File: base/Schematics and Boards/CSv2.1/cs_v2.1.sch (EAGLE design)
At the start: 80 parts, among them J101 J-JTAG-CORTEX-NEEDLE6-LEGS, J301 HIROSE-DF40_44-PIN_CONNECTORS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, J302 HIROSE-DF40_30-PIN_CONNECTORS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, Q201 FK3303010L, Q202 DMG3415UFY4Q-7F, Q203 FK3303010L, Q204 FK3303010L, U101 ATSAMD51, U102 AT25SF641-MHB-T, U201 COULOMB-MAX17262, U202 MAX77827BEWC+T, U203 SENSOR-SI7006, U204 LOADSWITCH-MIC94164, U205 LOADSWITCH-MIC94164, Y101 16M, Y102 ABS07-32.768KHZ-9-T

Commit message: Minor modifications from learnings of debug-board build
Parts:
- DTR, PROC, STOR, TEMP: value TPTP06R -> PTR1TP10SQ; device TestPoints:TPTP06R -> TestPoints:PTR1TP10SQ
- J301: value HIROSE-DF40_44-PIN_CONNECTORS-RECEPTACLE -> HIROSE-DF40_50-PIN_CONNECTORS-RECEPTACLE; device Connectors:HIROSE-DF40_44-PIN_CONNECTORS-RECEPTACLE -> Connectors:HIROSE-DF40_50-PIN_CONNECTORS-RECEPTACLE
- J302: value HIROSE-DF40_30-PIN_CONNECTORS-RECEPTACLE -> HIROSE-DF40_50-PIN_CONNECTORS-RECEPTACLE; device Connectors:HIROSE-DF40_30-PIN_CONNECTORS-RECEPTACLE -> Connectors:HIROSE-DF40_50-PIN_CONNECTORS-RECEPTACLE
- R206: value 1 -> 2.21; MANUFACTURER (none) -> Stackpole; PART_NO ERJ-3RQF1R0V -> RNCF0603BKC2R21; TOL 1% -> 0.1%
- R207: MANUFACTURER (none) -> Ohmite; PART_NO ERJ-3BQFR51V -> KDV06DR510ET; TOL 1% -> 0.5%
- R208: MANUFACTURER (none) -> KOA Speer; PART_NO ERJ-3RQF1R0V -> SR732BTTD1R00D; TOL 1% -> 0.5%
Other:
- note removed: "WS2812 or neopixel-like?? Maybe WS2812C-2020 (2x2mm) Require 5V input, so may need LED driver. Worth??"
- moved on the sheet: D202, JP202, Q201, Q203, Q204, R202, R203, R204

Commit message: Revision 2.1 of schematic for the CommonSense Main Board
Changes include (at the least): Removal LED NFETs, increase connector size to 50 pins w/ 4mm z-height, swap FLASH for a Winbond part with 1 Gbit NVM, change current measurement to include two daughter card channels, add LDO as alternative to buck-boost with gating solder jumpers, modify power-switching setup to use dual PFET (one is an extension of the mechanical switch to allow higher currents), total revamp of DTR/DBG card pin-mapping, and probably a few more small items. 

These changes are local to the schematic, for the most part. Changes to the board are minimal, but do include shifting the connector up, as well as the top-most drill-holes
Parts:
- removed C116, C117: 6.8p, Capacitors:C-0402
- removed DTR, PROC: PTR1TP10SQ, TestPoints:PTR1TP10SQ
- removed JP204: JUMPER-SMT_2_NC_PASTE_NO-SILK, Connectors:JUMPER-SMT_2_NC_PASTE_NO-SILK
- removed Q201, Q203, Q204: FK3303010L, Switches:FK3303010L
- removed Q202: DMG3415UFY4Q-7F, Switches:DMG3415UFY4Q-7F
- removed R205: 10, Resistors:R-0603
- removed RXDBG, TXDBG: TPTP06R, TestPoints:TPTP06R
- removed U102: AT25SF641-MHB-T, Storage:AT25SF641-MHB-T
- removed Y101: 16M, Oscillators:EPSON_TSX-3225_16.0000MF09Z-AC3
- added C1: 0.1u, Capacitors:C-0402
- added JP1, JP2: JUMPER-SMT_3_1-NC_PASTE_NO-SILK, SparkFun-Jumpers:JUMPER-SMT_3_1-NC_PASTE_NO-SILK
- added JP3, JP7: JUMPER-SMT_2_NC_PASTE_NO-SILK, Connectors:JUMPER-SMT_2_NC_PASTE_NO-SILK
- added JP4, JP5, JP6: JUMPER-SMT_2_NO_PASTEFREE, Connectors:JUMPER-SMT_2_NO_PASTEFREE
- added Q1: SIS903DN, Switches:SIS903DN
- added U1: NCP708MU330TAG, Regulators:LDO_ONSEMI_NCP708
- added U2: W25N01GVZEIG, Storage:W25N01GVZEIG
- added U3: TS3A24159YZPR, Switches:TS3A24159YZPR
- CPU, SCL, SDA: value TPTP06R -> PTR1TP10SQ; device TestPoints:TPTP06R -> TestPoints:PTR1TP10SQ
- D201: value CUS520H3F -> MBRM110ET1G; device Diodes:CUS520H3F -> Diodes:MBRM110ET1G
- J301: PART_NO DF40HC(3.0)-44DS-0.4V(51) -> DF40HC(4.0)-50DS-0.4V(51)
- J302: PART_NO DF40HC(3.0)-30DS-0.4V(58) -> DF40HC(4.0)-50DS-0.4V(58)
- R206: MPN (none) -> RNCF0603BKC2R21
- R207, R208: MPN (none) -> KDV06DR510ET
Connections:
- net DTR_V_SENSE- renamed DTR_MSTR_GPIO1
- removed net +3V3_DTR_SENSE: JP205.2, R207.2
- removed net +3V3_PROC_SENSE: JP204.2, R206.2
- removed net +3V3_STOR_SENSE: C206.1, J302.18, R208.2, U204.VIN
- removed net +3V3_TEMP_SENSE: C207.1, J302.20, R205.2, U205.VIN
- removed net DTR_BUS0_AIN0: J301.8, U101.PA2
- removed net DTR_BUS0_AIN1: J301.16, U101.PA3
- removed net DTR_BUS0_GPIO0: J301.24, U101.PB12
- removed net DTR_BUS0_GPIO1: J301.32, U101.PB13
- removed net DTR_BUS0_SERCOM0_P0: J301.7, U101.PA8
- removed net DTR_BUS0_SERCOM0_P1: J301.15, U101.PA9
- removed net DTR_BUS0_SERCOM0_P2: J301.23, U101.PA10
- removed net DTR_BUS0_SERCOM0_P3: J301.31, U101.PA11
- removed net DTR_BUS1_AIN0: J301.10, U101.PA4
- removed net DTR_BUS1_AIN1: J301.18, U101.PA5
- removed net DTR_BUS2_AIN0: J301.12, U101.PC2
- removed net DTR_BUS2_AIN1: J301.20, U101.PC3
- removed net DTR_BUS3_AIN0: J301.14, U101.PB4
- removed net DTR_BUS3_AIN1: J301.22, U101.PB5
- removed net DTR_BUS3_GPIO0: J301.30, U101.PA6
- removed net DTR_BUS3_GPIO1: J301.38, U101.PA7
- removed net DTR_BUS3_SERCOM7_P0: J301.13, U101.PD8
- removed net DTR_BUS3_SERCOM7_P1: J301.21, U101.PD9
- removed net DTR_BUS3_SERCOM7_P2: J301.29, U101.PD10
- removed net DTR_BUS3_SERCOM7_P3: J301.37, U101.PD11
- removed net DTR_DETECT: J301.39, U101.PA21
- removed net DTR_MASTER_I2C_SCL: J301.40, R103.1, SCL.TP, U101.PA23, U201.SCL, U203.SCL
- removed net DTR_MASTER_I2C_SDA: J301.42, R104.1, SDA.TP, U101.PA22, U201.SDA, U203.SDA
- removed net DTR_MASTER_IRQ: J301.44
- removed net N$16: Q203.D, R203.2
- removed net STOR_HOLD: U101.PB7, U102.NHOLD/IO3
- removed net STOR_SPI5_MISO: U101.PB3, U102.SO/IO1
- removed net STOR_SPI5_MOSI: U101.PB0, U102.SI/IO0
- removed net STOR_SPI5_NCS: U101.PB2, U102.NCS
- removed net STOR_SPI5_SCK: U101.PB1, U102.SCK
- removed net STOR_WP: U101.PB6, U102.WP/IO2
- removed net VDD_DBG: J302.2, J302.4, JP201.2
- removed net VDD_SW_IN: JP203.2, S201.P
- removed net XIN: C116.1, U101.PB22, Y101.1
- removed net XOUT: C117.1, U101.PB23, Y101.3
- new net +3V3_DTR_SENSE-: JP205.2, JP5.2, R207.2, U3.COM1, U3.NC1, U3.NC2
- new net DBG_DTR_V_SENSE: J301.8, J302.18
- new net DBG_DTR_V_SENSE_EX: J302.20, U3.COM2
- new net DBG_GPIO10: J302.40, U101.PB28
- new net DBG_GPIO11: J302.38, U101.PB29
- new net DBG_GPIO4/SERCOM6_P0: J302.30, U101.PC16
- new net DBG_GPIO5/SERCOM6_P1: J302.32, U101.PC17
- new net DBG_GPIO6/SERCOM6_P2: J302.34, U101.PC18
- new net DBG_GPIO7/SERCOM6_P3: J302.36, U101.PC19
- new net DBG_GPIO8: J302.44, U101.PB26
- new net DBG_GPIO9: J302.42, U101.PB27
- new net DBG_PROC_V_SENSE: J302.16, JP6.2, JP7.2, R206.2
- new net DBG_STOR_V_SENSE: C206.1, J302.22, JP4.2, R208.2, U204.VIN
- new net DBG_VDD: J302.2, J302.4, J302.6, JP201.2
- new net DTR_BUS0_AIN0/GPIO2: J301.7, U101.PA2
- new net DTR_BUS0_AIN1/GPIO3: J301.9, U101.PA3
- new net DTR_BUS0_GPIO0/I2S_SCK0: J301.19, U101.PB16
- new net DTR_BUS0_GPIO1/I2S_MCK0: J301.21, U101.PB17
- new net DTR_BUS0_SERCOM5_P0/I2S_FS1: J301.42, U101.PA23
- new net DTR_BUS0_SERCOM5_P1/I2S_SDI: J301.40, U101.PA22
- new net DTR_BUS0_SERCOM5_P2/I2S_FS0: J301.30, U101.PA20
- new net DTR_BUS0_SERCOM5_P3/I2S_SDO: J301.28, U101.PA21
- new net DTR_BUS1_AIN0/GPIO2: J301.11, U101.PA4
- new net DTR_BUS1_AIN1/GPIO3: J301.13, U101.PA5
- new net DTR_BUS2_AIN0/GPIO2: J301.15, U101.PC2
- new net DTR_BUS2_AIN1/GPIO3: J301.17, U101.PC3
- new net DTR_DETECT/DTR_IRQ0/SERCOM7_P2: J301.16, U101.PD10
- new net DTR_IRQ1/SERCOM7_P3: J301.18, U101.PD11
- new net DTR_MSTR_GPIO0: J301.41, U101.PC15
- new net DTR_MSTR_GPIO_1: U101.PC20
- new net DTR_MSTR_I2C_SCL_SERCOM7_P1: J301.14, R103.1, SCL.TP, U101.PD9, U201.SCL, U203.SCL
- new net DTR_MSTR_I2C_SDA_SERCOM7_P0: J301.12, R104.1, SDA.TP, U101.PD8, U201.SDA, U203.SDA
- new net DTR_MSTR_SPI_CSS0_SERCOM3_P2: J301.37, U101.PD20
- new net DTR_MSTR_SPI_CSS1: J301.31, U101.PD12
- new net DTR_MSTR_SPI_MISO_SERCOM3_P3: J301.39, U101.PD21
- new net DTR_MSTR_SPI_MOSI_SERCOM3_P0: J301.33, U101.PC23
- new net DTR_MSTR_SPI_SCK_SERCOM3_P1: J301.35, U101.PC22
- new net DTR_SENSE_SW: U101.PC7, U3.IN1, U3.IN2
- new net DTR_V_SENSE_EX: J301.10, U3.NO2
- new net N$11: Q1.G2, S201.P
- new net N$3: JP2.1, U202.OUT, U202.OUTS
- new net N$7: JP1.3, U1.EN, U1.IN
- new net N$8: JP203.2, Q1.D2, S201.O
- new net STOR_QSPI_CK: U101.PB10, U2.CLK
- new net STOR_QSPI_CS: U101.PB11, U2./CS
- new net STOR_QSPI_D0: U101.PA8, U2.DI(IO0)
- new net STOR_QSPI_D1: U101.PA9, U2.DO(IO1)
- new net STOR_QSPI_D2: U101.PA10, U2./WP(IO2)
- new net STOR_QSPI_D3: U101.PA11, U2./HOLD(IO3)
- new net VREG_BB_IN: JP1.1, U202.EN, U202.IN
- net +3V3: now also C207.1, J302.14, JP2.2, JP3.2, JP4.1, JP5.1, JP6.1, U205.VIN, U3.NO1; no longer J302.12, R205.1, U202.OUT, U202.OUTS
- net +3V3_DTR: no longer DTR.TP, J302.16
- net +3V3_PROC: now also JP7.1; no longer J302.14, JP204.1, PROC.TP
- net +3V3_STOR: now also U2.VCC; no longer U102.VDD
- net +3V7_BATT: now also J302.12, JP203.1, Q1.D1; no longer J302.6, JP203.3, Q202.D
- net CC_IN: now also Q1.S2; no longer S201.O
- net DBG_GPIO0: now also J302.31, U101.PB22; no longer J302.7, U101.PC16
- net DBG_GPIO1: now also J302.29, U101.PB23; no longer J302.9, U101.PC17
- net DBG_GPIO2: now also J302.27, U101.PB24; no longer J302.11, U101.PC18
- net DBG_GPIO3: now also J302.25, U101.PB25; no longer J302.13, U101.PC19
- net DBG_SERIAL_RX_SERCOM4: now also J302.9; no longer J302.17, RXDBG.TP
- net DBG_SERIAL_TX_SERCOM4: now also J302.11; no longer J302.15, TXDBG.TP
- net DBG_SWCLK: now also J302.28; no longer J302.19
- net DBG_SWDIO: now also J302.26; no longer J302.21
- net DBG_TRACE_CLK: now also J302.23; no longer J302.26
- net DBG_TRACE_D0: now also J302.15; no longer J302.23
- net DBG_TRACE_D1: now also J302.17; no longer J302.25
- net DBG_TRACE_D2: now also J302.19; no longer J302.27
- net DBG_TRACE_D3: now also J302.21; no longer J302.29
- net DBG_TRACE_SWO: now also J302.13; no longer J302.28
- net DBG_USB_D_N: now also J302.49; no longer J302.22
- net DBG_USB_D_P: now also J302.47; no longer J302.24
- net DTR_BUS1_GPIO0: now also J301.23, U101.PC11; no longer J301.26, U101.PB14
- net DTR_BUS1_GPIO1: now also J301.25, U101.PC12; no longer J301.34, U101.PB15
- net DTR_BUS1_SERCOM1_P0: now also J301.38; no longer J301.9
- net DTR_BUS1_SERCOM1_P1: now also J301.36; no longer J301.17
- net DTR_BUS1_SERCOM1_P2: now also J301.26; no longer J301.25
- net DTR_BUS1_SERCOM1_P3: now also J301.24; no longer J301.33
- net DTR_BUS2_GPIO0: now also J301.27, U101.PC13; no longer J301.28, U101.PB16
- net DTR_BUS2_GPIO1: now also J301.29, U101.PC14; no longer J301.36, U101.PB17
- net DTR_BUS2_SERCOM2_P0: now also J301.34; no longer J301.11
- net DTR_BUS2_SERCOM2_P1: now also J301.32; no longer J301.19
- net DTR_BUS2_SERCOM2_P2: now also J301.22; no longer J301.27
- net DTR_BUS2_SERCOM2_P3: now also J301.20; no longer J301.35
- net EN_TEMP: now also U101.PB2; no longer U101.PB25
- net GND: now also C1.2, J302.7, S201.S, U1.GND, U2.GND, U2.GND_2, U3.GND; no longer C116.2, C117.2, Q201.S, Q203.S, Q204.S, U102.GND, Y101.1_GND, Y101.2_GND
- net LED_B: now also R202.2, U101.PB18; no longer Q201.G, U101.PB28
- net LED_G: now also R203.2, U101.PB19; no longer Q203.G, U101.PB27
- net LED_R: now also R204.2, U101.PB20; no longer Q204.G, U101.PB26
- net N$15: now also JP2.3, U1.OUT; no longer Q201.D, R202.2
- net N$17: now also C1.1, JP3.1, U3.V+; no longer Q204.D, R204.2
- net NRESET: now also J302.24; no longer J302.30
- net VDD_DBG_JMP: now also Q1.G1; no longer Q202.G
- net VDD_SW: now also JP203.3, Q1.S1; no longer JP203.1, Q202.S
- net VREG_IN: now also JP1.2; no longer U202.EN, U202.IN
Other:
- note added: "Analog switch to allow the daughter card to pass down the low side of the voltage it wants read. A single select line is used to either sense all current across all DTR cards OR just a portion."
- note added: "Buck-boost"
- note added: "Dual-Regulators High-side current monitors for high frequency (~100kHz) current measurementis not possible with a switching regulator (buck-boost). We add a secondary reg (LDO) which can be enabledby making the proper connections with solder jumpers on either side. Both regulators should be very close to each other to maintain short distance to decoupling caps."
- note added: "Fast crystal removed, as it serves little advantage in addition to the 32k crystal"
- note added: "LDO"
- note added: "Ugly due to Dual PFET, sorry\! FET used to increased switch current capacity becauses most low-profile handle 0.3A abs. max. Mech. Switch still handles off/off by controlling the gate voltage. This is P-ch, so GND side will open the flood gates."
- note removed: "16 MHz Oscillator"
- note removed: "Buck-boost convertor"
- note removed: "Do we lose info about battery by not having the input directly connected to the battery?"
- note removed: "Won't always populate PMOS in deployements"
- moved on the sheet: C202, C205, C206, C207, C208, C209, D201, JP203, JP205, R206, R207, R208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

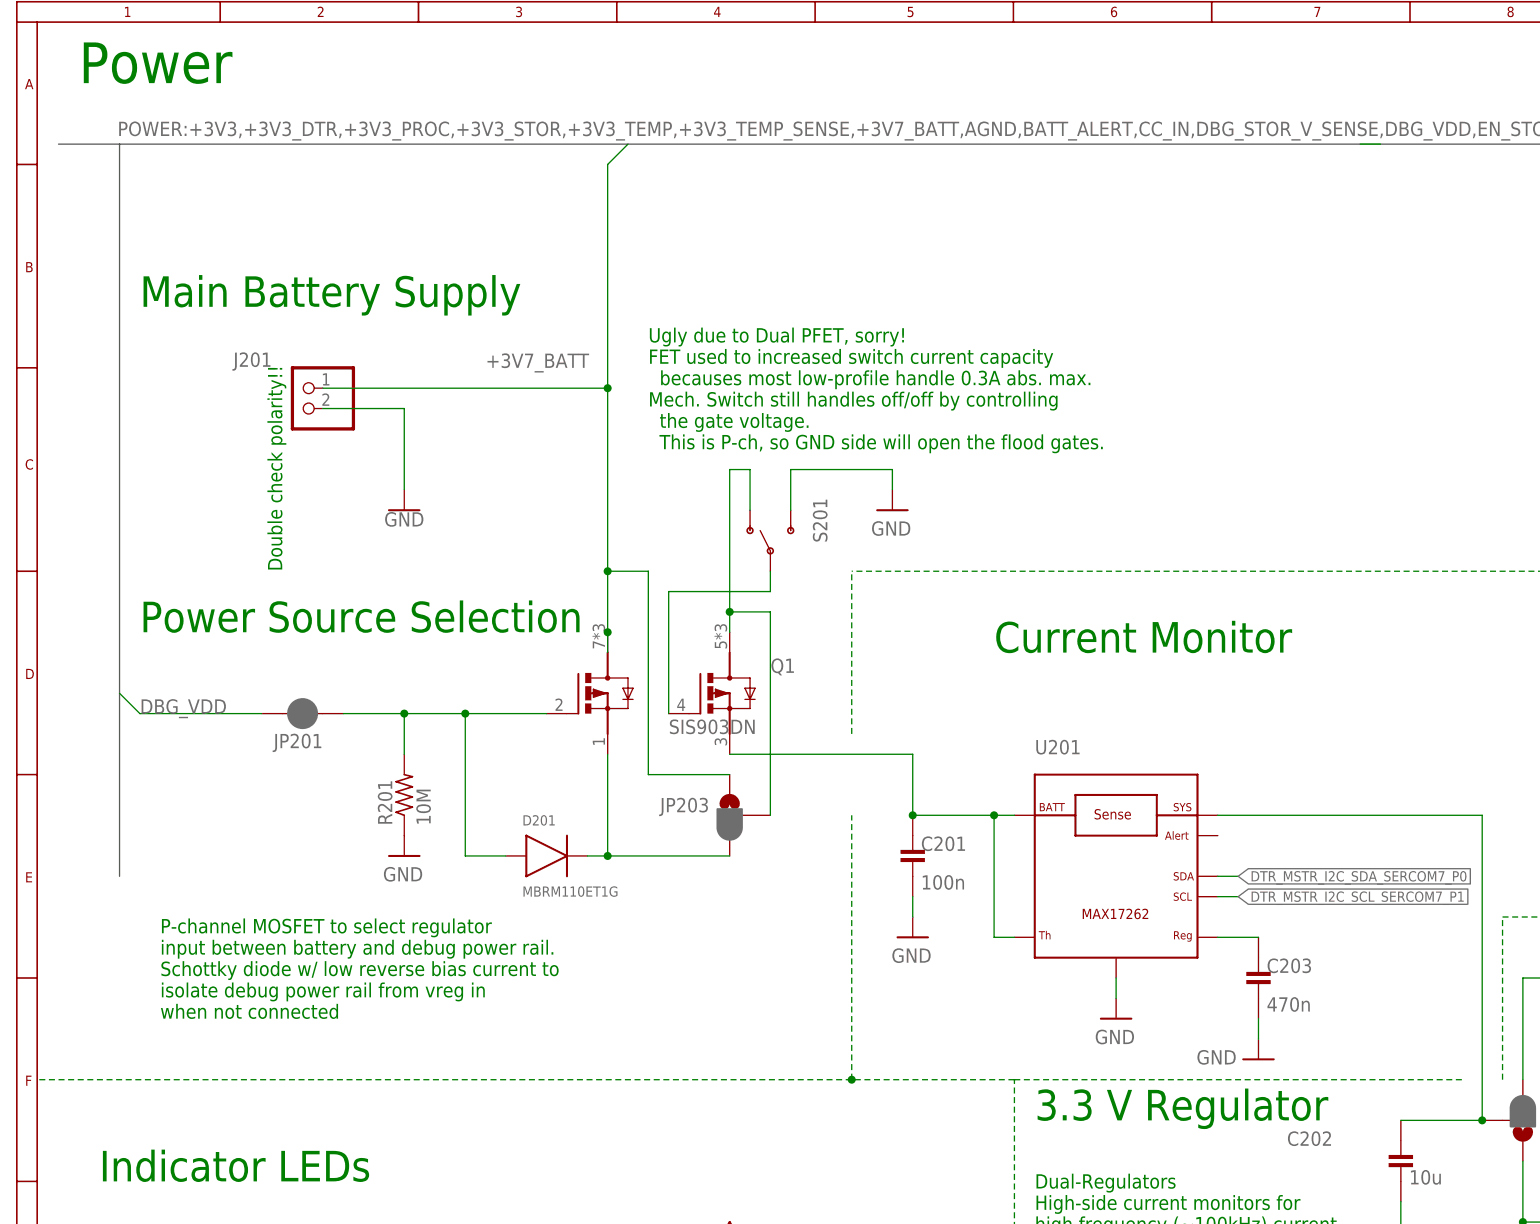
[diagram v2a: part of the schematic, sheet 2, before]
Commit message: Upgrade power selection on main board from PFET -> 2:1 power mux
Testing on CSmain 2.0 showed some disturbing changes in voltage across the PFET (most likely due to an device physics imposing a typical Vgs threshold before conducting well) that would make the LDO on the board unusable if only a LiPo battery was available. For boards that will need power switching between main board source and debug-board source, we need something more sophisticated. 

Also included is a load switch whose enable is controlled by a mechanical switch. This should be more trustworthy than a PFET, and can conduct substantially more current than the mechanical switch alone.
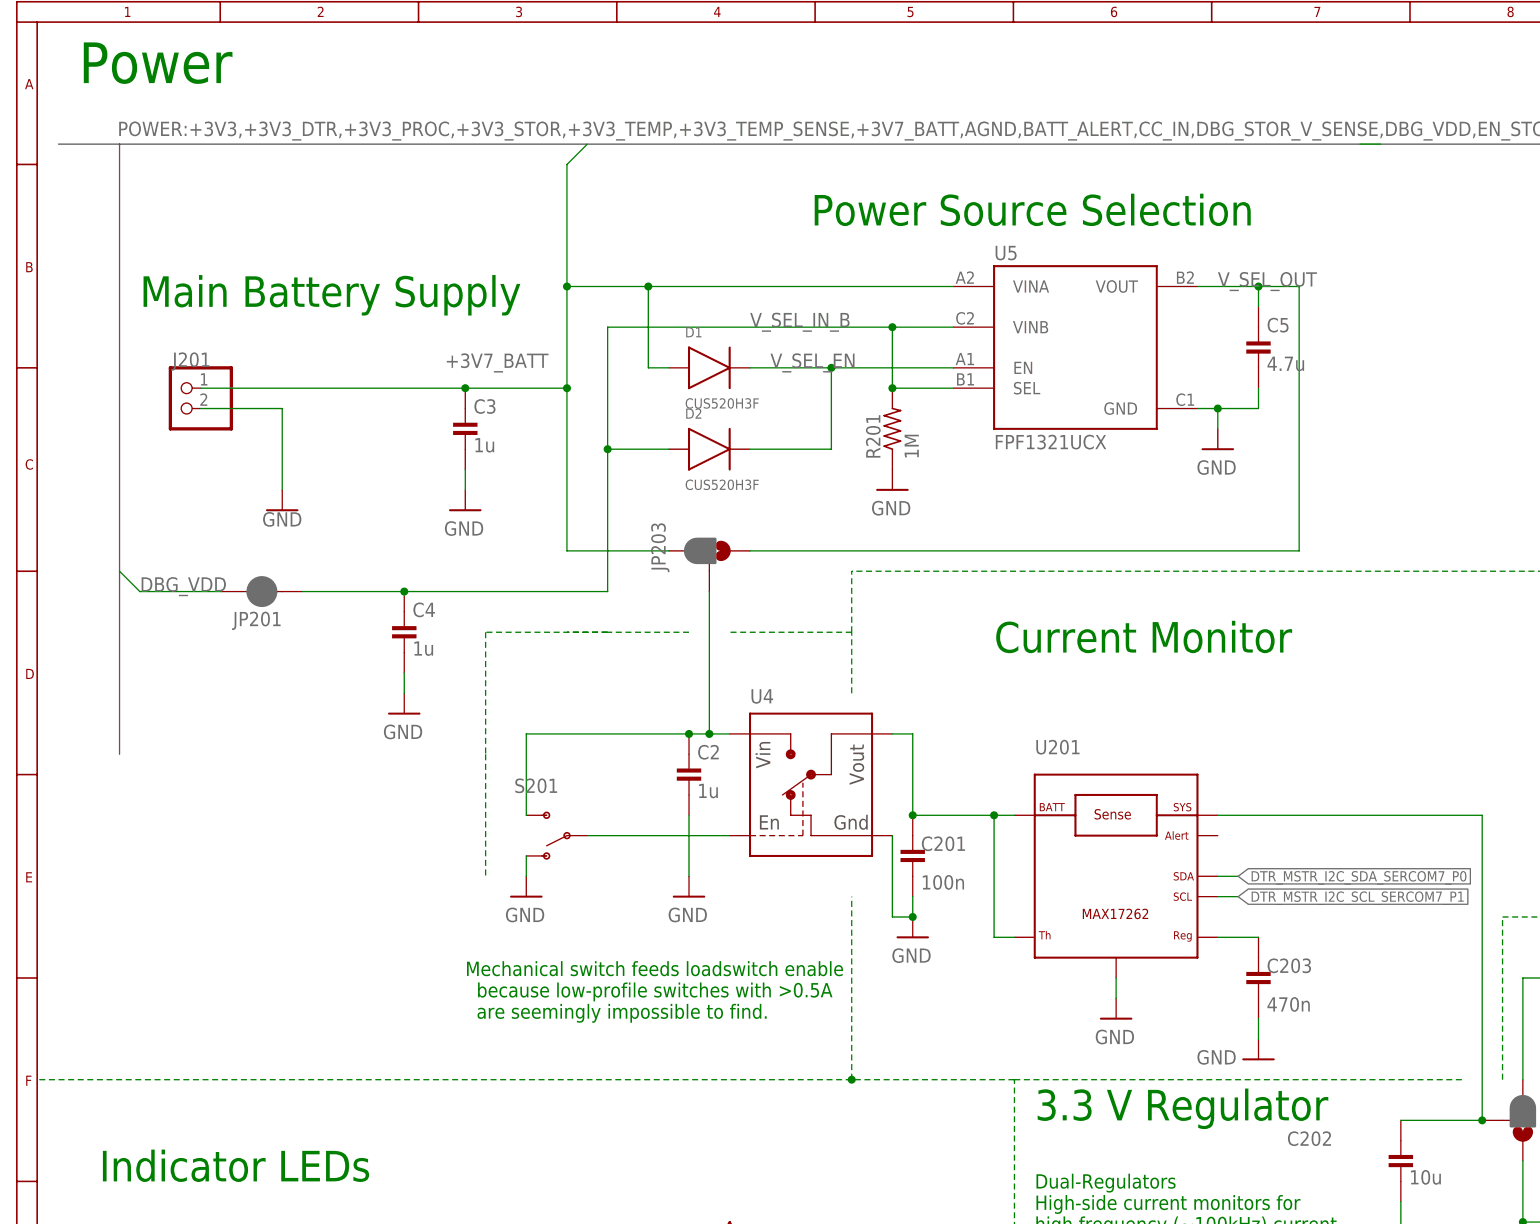
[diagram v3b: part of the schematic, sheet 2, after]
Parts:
- removed D201: MBRM110ET1G, Diodes:MBRM110ET1G
- removed Q1: SIS903DN, Switches:SIS903DN
- added C2, C3, C4: 1u, Capacitors:C-0402
- added C5: 4.7u, Capacitors:C-0805
- added D1, D2: CUS520H3F, Diodes:CUS520H3F
- added U4: LOADSWITCH-MIC94164, Switches:LOADSWITCH-MIC94164
- added U5: FPF1321UCX, Switches:FPF1321UCX
- R201: value 10M -> 1M; MPN (none) -> ERJ-2GEJ105X; PART_NO ERJ-2GEJ106X -> ERJ-2GEJ105X
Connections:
- removed net VDD_DBG_JMP: D201.P, JP201.1, Q1.G1, R201.2
- removed net VDD_SW: D201.N, JP203.3, Q1.S1
- new net V_SEL_EN: D1.N, D2.N, U5.EN
- new net V_SEL_IN_B: C4.1, D2.P, JP201.1, R201.2, U5.SEL, U5.VINB
- new net V_SEL_OUT: C5.1, JP203.1, U5.VOUT
- net +3V7_BATT: now also C3.1, D1.P, JP203.3, U5.VINA; no longer JP203.1, Q1.D1
- net CC_IN: now also U4.VOUT; no longer Q1.S2
- net GND: now also C2.2, C3.2, C4.2, C5.2, S201.O, U4.GND, U5.GND; no longer S201.S
- net N$11: now also U4.ENABLE; no longer Q1.G2
- net N$8: now also C2.1, S201.S, U4.VIN; no longer Q1.D2, S201.O
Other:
- note added: "Mechanical switch feeds loadswitch enable because low-profile switches with >0.5A are seemingly impossible to find."
- note removed: "Double check polarity!!"
- note removed: "P-channel MOSFET to select regulator input between battery and debug power rail. Schottky diode w/ low reverse bias current to isolate debug power rail from vreg in when not connected"
- note removed: "Ugly due to Dual PFET, sorry\! FET used to increased switch current capacity becauses most low-profile handle 0.3A abs. max. Mech. Switch still handles off/off by controlling the gate voltage. This is P-ch, so GND side will open the flood gates."
- moved on the sheet: J201, JP201, JP203, R201, S201

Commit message: Swap daughter card v-sense pins
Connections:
- removed net DBG_DTR_V_SENSE: J301.8, J302.18
- removed net DBG_DTR_V_SENSE_EX: J302.20, U3.COM2
- removed net DTR_V_SENSE_EX: J301.10, U3.NO2
- new net DBG_DTR0_V_SENSE: J302.18, U3.COM2
- new net DBG_DTR1_V_SENSE: J301.10, J302.20
- new net DTR_DTR0_V_SENSE: J301.8, U3.NO2

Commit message: Finished schematic revision for main, debug boards.
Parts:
- removed C3, C4: 1u, Capacitors:C-0402
- removed C5: 4.7u, Capacitors:C-0805
- removed D1, D2: CUS520H3F, Diodes:CUS520H3F
- removed JP4, JP5, JP6: JUMPER-SMT_2_NO_PASTEFREE, Connectors:JUMPER-SMT_2_NO_PASTEFREE
- removed R201: 1M, Resistors:R-0402
- added Q1: DMG3415UFY4Q-7F, Switches:DMG3415UFY4Q-7F
- added R1: 510k, Resistors:R-0402
- U5: value FPF1321UCX -> PD3S140-7; device Switches:FPF1321UCX -> Diodes:PD3S140-7
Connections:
- net DBG_TRACE_CLK renamed DBG_TRACE_CLK/GPIO17
- net DBG_TRACE_D0 renamed DBG_TRACE_D0/GPIO13
- net DBG_TRACE_D1 renamed DBG_TRACE_D1/GPIO14
- net DBG_TRACE_D2 renamed DBG_TRACE_D2/GPIO15
- net DBG_TRACE_D3 renamed DBG_TRACE_D3/GPIO16
- net DBG_TRACE_SWO renamed DBG_TRACE_SWO/GPIO12
- net N$11 renamed V.SRC.EN
- net N$8 renamed V.SRC
- removed net V_SEL_EN: D1.N, D2.N, U5.EN
- removed net V_SEL_OUT: C5.1, JP203.1, U5.VOUT
- new net +3V3_DTR.SW: JP205.2, U3.COM1
- new net N$2: JP203.3, Q1.S, U5.N
- net +3V3: no longer JP4.1, JP5.1, JP6.1
- net +3V3_DTR_SENSE-: no longer JP205.2, JP5.2, U3.COM1
- net +3V7_BATT: now also JP203.1, Q1.D; no longer C3.1, D1.P, JP203.3, U5.VINA
- net DBG_PROC_V_SENSE: no longer JP6.2
- net DBG_STOR_V_SENSE: no longer JP4.2
- net GND: now also R1.1; no longer C3.2, C4.2, C5.2, R201.1, S201.O, U5.GND
- net V_SEL_IN_B: now also Q1.G, R1.2, U5.P; no longer C4.1, D2.P, R201.2, U5.SEL, U5.VINB
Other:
- note added: "Oscillator"
- note added: "Replace sense resisitor with 0Ω for designs where power is essential"
- note added: "Switch has 300-500 mΩ resistance!"
- note removed: "Fast crystal removed, as it serves little advantage in addition to the 32k crystal"
- note removed: "Oscillators"
- moved on the sheet: C118, C119, C2, C205, J201, JP203, U4, Y102
